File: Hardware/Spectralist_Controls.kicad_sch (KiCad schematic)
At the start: 30 parts, among them J1 Conn_01x8_Pin, J10 FilterA_CV, J11 FilterB_CV, J12 ChannelAOut, J13 ChannelBOut, J14 Conn_01x03_Pin, J15 Conn_01x02_Pin, J16 Conn_01x02_Pin, J2 Conn_01x8_Pin, J3 Conn_01x10_Pin, J4 Conn_01x10_Pin, J5 StretchCV, J6 VOctCV, J7 WarpCV, J8 PanCV, J9 SlopeCV, SW1 Harmonic_Switch, SW2 Filter_Switch, SW3 B_Octave

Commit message: Hardware fixes
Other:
- note added: "Panel Errata: Mode switch hole too large for subminiature switch"
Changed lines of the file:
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@@
+		)
+	)
+	(text "Panel Errata: Mode switch hole too large for subminiature switch"
+		(exclude_from_sim no)
+		(at 212.598 170.434 0)
+		(effects
+			(font
+				(size 1.27 1.27)
+			)
 		)
 	)
@@
 	(label "Filter_Slope_Pot"
 		(at 157.48 113.03 0)
-		(fields_autoplaced yes)
 		(effects
 			(font
@@
 	(label "LED_SCL"
 		(at 200.66 43.18 0)
-		(fields_autoplaced yes)
 		(effects
 			(font
@@
 	(label "Harm_Warp_CV_In"
 		(at 265.43 96.52 0)
-		(fields_autoplaced yes)
 		(effects
 			(font
@@
 	(label "LED_Oct_Out"
 		(at 227.33 52.07 0)
-		(fields_autoplaced yes)
 		(effects
 			(font
@@
 	(label "Filter_A_Pot"
 		(at 115.57 30.48 0)
-		(fields_autoplaced yes)
 		(effects
 			(font
@@
 	(label "Harm_Warp_CV_In"
 		(at 35.56 71.12 0)
-		(fields_autoplaced yes)
 		(effects
 			(font
@@
 	(label "Filter_A_CV_In"
 		(at 68.58 29.21 0)
-		(fields_autoplaced yes)
 		(effects
 			(font
@@
 	(label "Harm_Stretch_Trm"
 		(at 157.48 85.09 0)
-		(fields_autoplaced yes)
 		(effects
 			(font
@@
 	(label "Filter_B_CV_In"
 		(at 68.58 50.8 0)
-		(fields_autoplaced yes)
 		(effects
 			(font
@@
 	(label "Octave_Btn"
 		(at 129.54 170.18 180)
-		(fields_autoplaced yes)
 		(effects
 			(font
@@
 	(label "Filter_Mode"
 		(at 265.43 41.91 0)
-		(fields_autoplaced yes)
 		(effects
 			(font
@@
 	(label "Filter_Mode"
 		(at 83.82 170.18 180)
-		(fields_autoplaced yes)
 		(effects
 			(font
@@
 	(label "Pan_CV_In"
 		(at 35.56 95.25 0)
-		(fields_autoplaced yes)
 		(effects
 			(font
@@
 	(label "Harm_Stretch_CV_In"
 		(at 265.43 83.82 0)
-		(fields_autoplaced yes)
 		(effects
 			(font
@@
 	(label "Harm_Stretch_Pot"
 		(at 115.57 85.09 0)
-		(fields_autoplaced yes)
 		(effects
 			(font
@@
 	(label "LED_Filter_B_Out"
 		(at 205.74 149.86 180)
-		(fields_autoplaced yes)
 		(effects
 			(font
@@
 	(label "Harm_Stretch_Pot"
 		(at 227.33 101.6 0)
-		(fields_autoplaced yes)
 		(effects
 			(font
@@
 	(label "Harmonic_Mode"
 		(at 39.37 170.18 180)
-		(fields_autoplaced yes)
 		(effects
 			(font
@@
 	(label "Audio_Out_R"
 		(at 68.58 95.25 0)
-		(fields_autoplaced yes)
 		(effects
 			(font
@@
 	(label "Filter_B_Trm"
 		(at 227.33 78.74 0)
-		(fields_autoplaced yes)
 		(effects
 			(font
@@
 	(label "LED_Filter_A_Out"
 		(at 205.74 143.51 180)
-		(fields_autoplaced yes)
 		(effects
 			(font
@@
 	(label "Filter_A_Trm"
 		(at 157.48 30.48 0)
-		(fields_autoplaced yes)
 		(effects
 			(font
@@
 	(label "Octave_Btn"
 		(at 265.43 49.53 0)
-		(fields_autoplaced yes)
 		(effects
 			(font
@@
 	(label "Filter_A_Pot"
 		(at 265.43 52.07 0)
-		(fields_autoplaced yes)
 		(effects
 			(font
@@
 	(label "Filter_A_CV_In"
 		(at 265.43 93.98 0)
-		(fields_autoplaced yes)
 		(effects
 			(font
@@
 	(label "Filter_B_Pot"
 		(at 227.33 88.9 0)
-		(fields_autoplaced yes)
 		(effects
 			(font
@@
 	(label "LED_Filter_A_Out"
 		(at 227.33 49.53 0)
-		(fields_autoplaced yes)
 		(effects
 			(font
@@
 	(label "LED_Filter_B_Out"
 		(at 227.33 57.15 0)
-		(fields_autoplaced yes)
 		(effects
 			(font
@@
 	(label "Audio_Out_L"
 		(at 68.58 71.12 0)
-		(fields_autoplaced yes)
 		(effects
 			(font
@@
 	(label "Harm_Warp_Pot"
 		(at 115.57 113.03 0)
-		(fields_autoplaced yes)
 		(effects
 			(font
@@
 	(label "Filter_B_Pot"
 		(at 157.48 57.15 0)
-		(fields_autoplaced yes)
 		(effects
 			(font
@@
 	(label "LED_SCL"
 		(at 227.33 41.91 0)
-		(fields_autoplaced yes)
 		(effects
 			(font
@@
 	(label "Harm_Warp_Pot"
 		(at 227.33 96.52 0)
-		(fields_autoplaced yes)
 		(effects
 			(font
@@
 	(label "Pan_CV_In"
 		(at 265.43 99.06 0)
-		(fields_autoplaced yes)
 		(effects
 			(font
@@
 	(label "Harm_Stretch_CV_In"
 		(at 35.56 29.21 0)
-		(fields_autoplaced yes)
 		(effects
 			(font
@@
 	(label "LED_SDA"
 		(at 200.66 48.26 0)
-		(fields_autoplaced yes)
 		(effects
 			(font
@@
 	(label "Filter_B_CV_In"
 		(at 265.43 101.6 0)
-		(fields_autoplaced yes)
 		(effects
 			(font
@@
 	(label "Filter_A_Trm"
 		(at 265.43 54.61 0)
-		(fields_autoplaced yes)
 		(effects
 			(font
@@
 	(label "Filter_Slope_CV_In"
 		(at 265.43 88.9 0)
-		(fields_autoplaced yes)
 		(effects
 			(font
@@
 	(label "Filter_Slope_Pot"
 		(at 227.33 91.44 0)
-		(fields_autoplaced yes)
 		(effects
 			(font
@@
 	(label "LED_SDA"
 		(at 227.33 44.45 0)
-		(fields_autoplaced yes)
 		(effects
 			(font
@@
 	(label "Pitch_CV_In"
 		(at 265.43 86.36 0)
-		(fields_autoplaced yes)
 		(effects
 			(font
@@
 	(label "Filter_Slope_CV_In"
 		(at 35.56 118.11 0)
-		(fields_autoplaced yes)
 		(effects
 			(font
@@
 	(label "LED_Oct_Out"
 		(at 205.74 156.21 180)
-		(fields_autoplaced yes)
 		(effects
 			(font
@@
 	(label "Harm_Stretch_Trm"
 		(at 227.33 99.06 0)
-		(fields_autoplaced yes)
 		(effects
 			(font
@@
 	(label "Audio_Out_L"
 		(at 227.33 81.28 0)
-		(fields_autoplaced yes)
 		(effects
 			(font
@@
 	(label "Pitch_CV_In"
 		(at 35.56 50.8 0)
-		(fields_autoplaced yes)
 		(effects
 			(font
@@
 	(label "Filter_B_Trm"
 		(at 115.57 57.15 0)
-		(fields_autoplaced yes)
 		(effects
 			(font
@@
 	(label "Audio_Out_R"
 		(at 227.33 86.36 0)
-		(fields_autoplaced yes)
 		(effects
 			(font
@@
 	(label "Harmonic_Mode"
 		(at 265.43 44.45 0)
-		(fields_autoplaced yes)
-		(effects
-			(font
+		(effects
+			(font

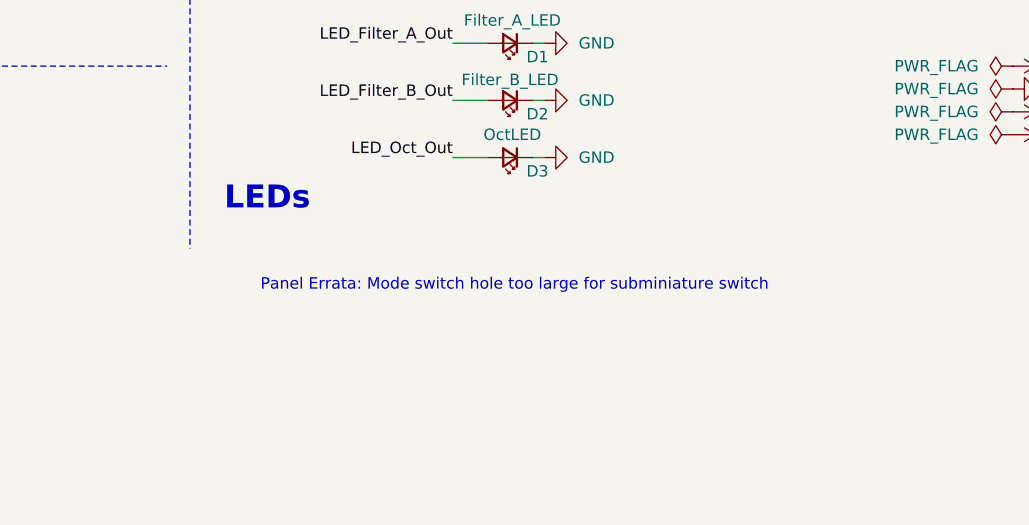
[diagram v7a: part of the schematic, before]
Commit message: Implemented Filter LEDs and Octave down button/LED
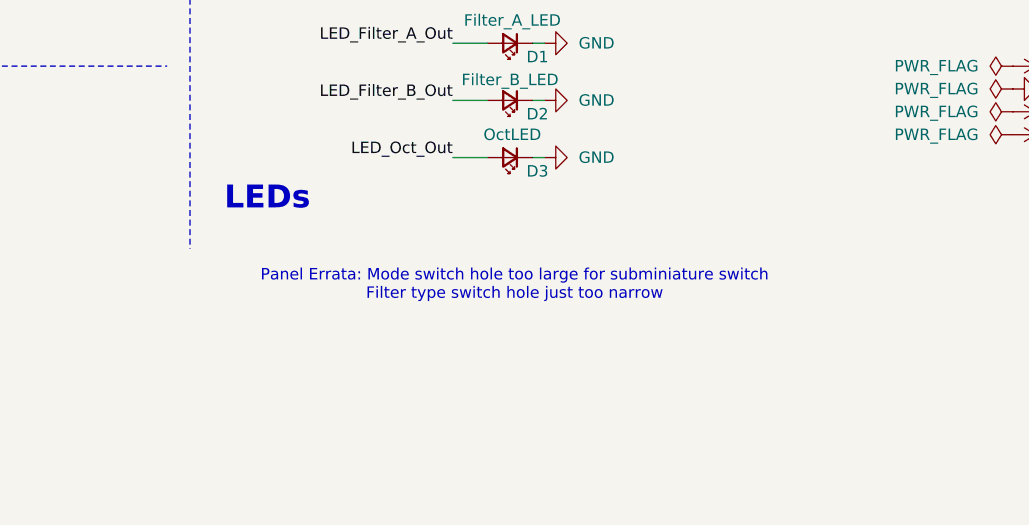
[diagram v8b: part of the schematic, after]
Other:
- note added: "Panel Errata: Mode switch hole too large for subminiature switch Filter type switch hole just too narrow"
- note removed: "Panel Errata: Mode switch hole too large for subminiature switch"
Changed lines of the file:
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@@
 		)
 	)
-	(text "Panel Errata: Mode switch hole too large for subminiature switch"
+	(text "Panel Errata: Mode switch hole too large for subminiature switch\nFilter type switch hole just too narrow"
 		(exclude_from_sim no)
 		(at 212.598 170.434 0)
